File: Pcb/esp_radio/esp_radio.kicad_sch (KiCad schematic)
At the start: 0 parts

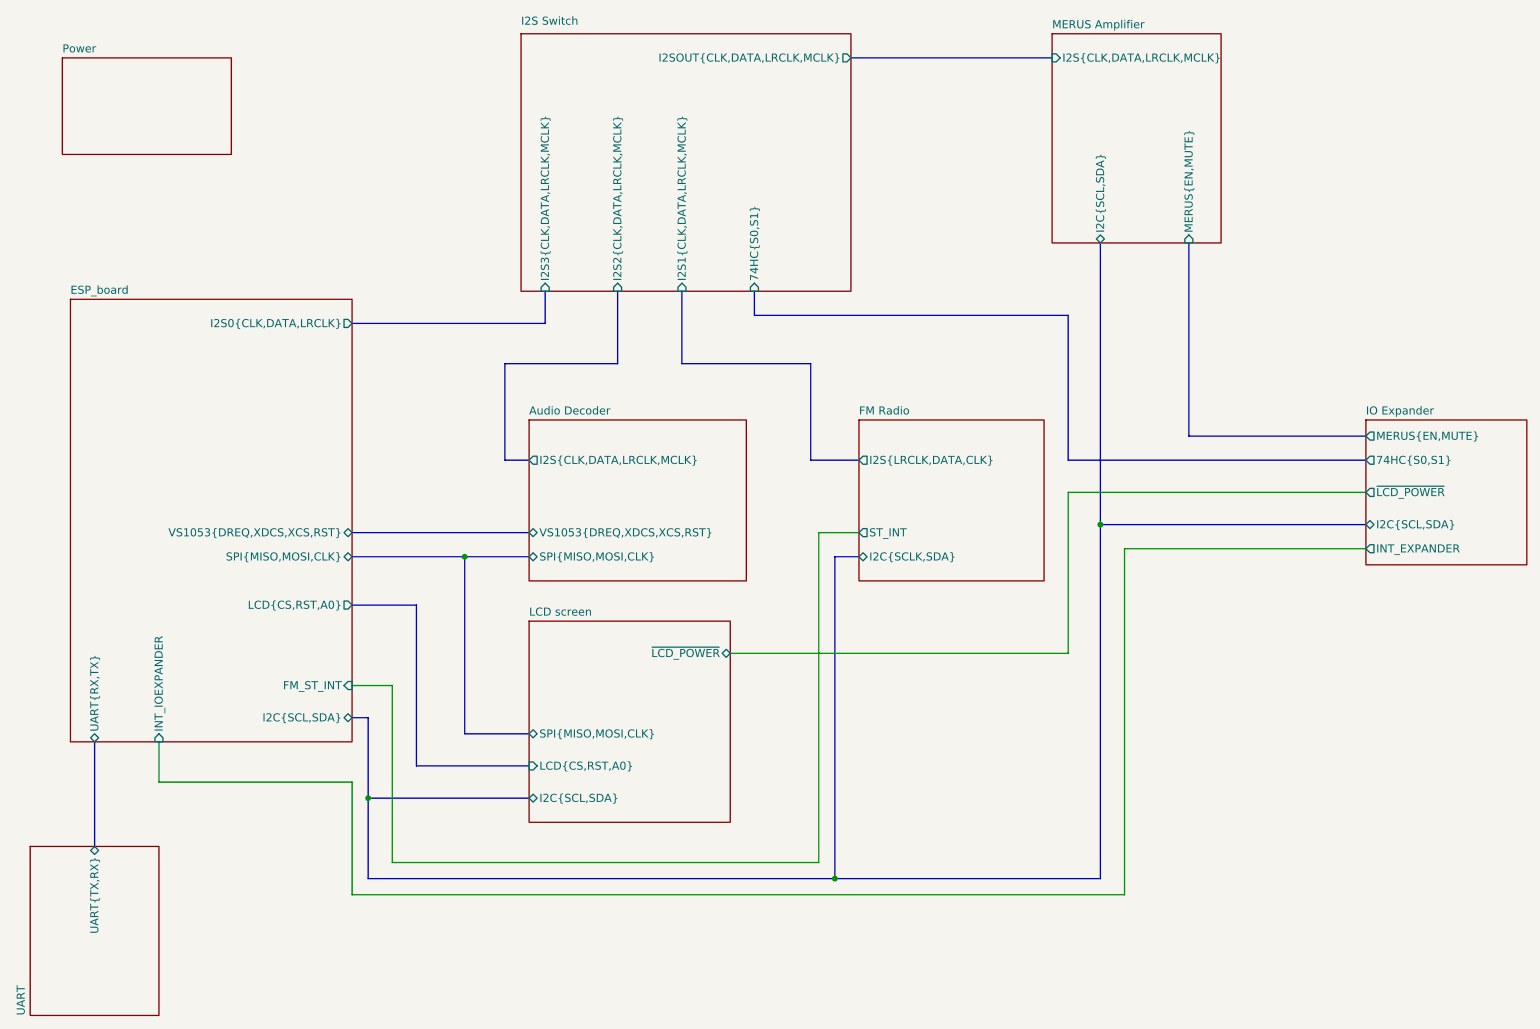
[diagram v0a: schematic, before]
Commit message: Move custom components to kicad_common_library.
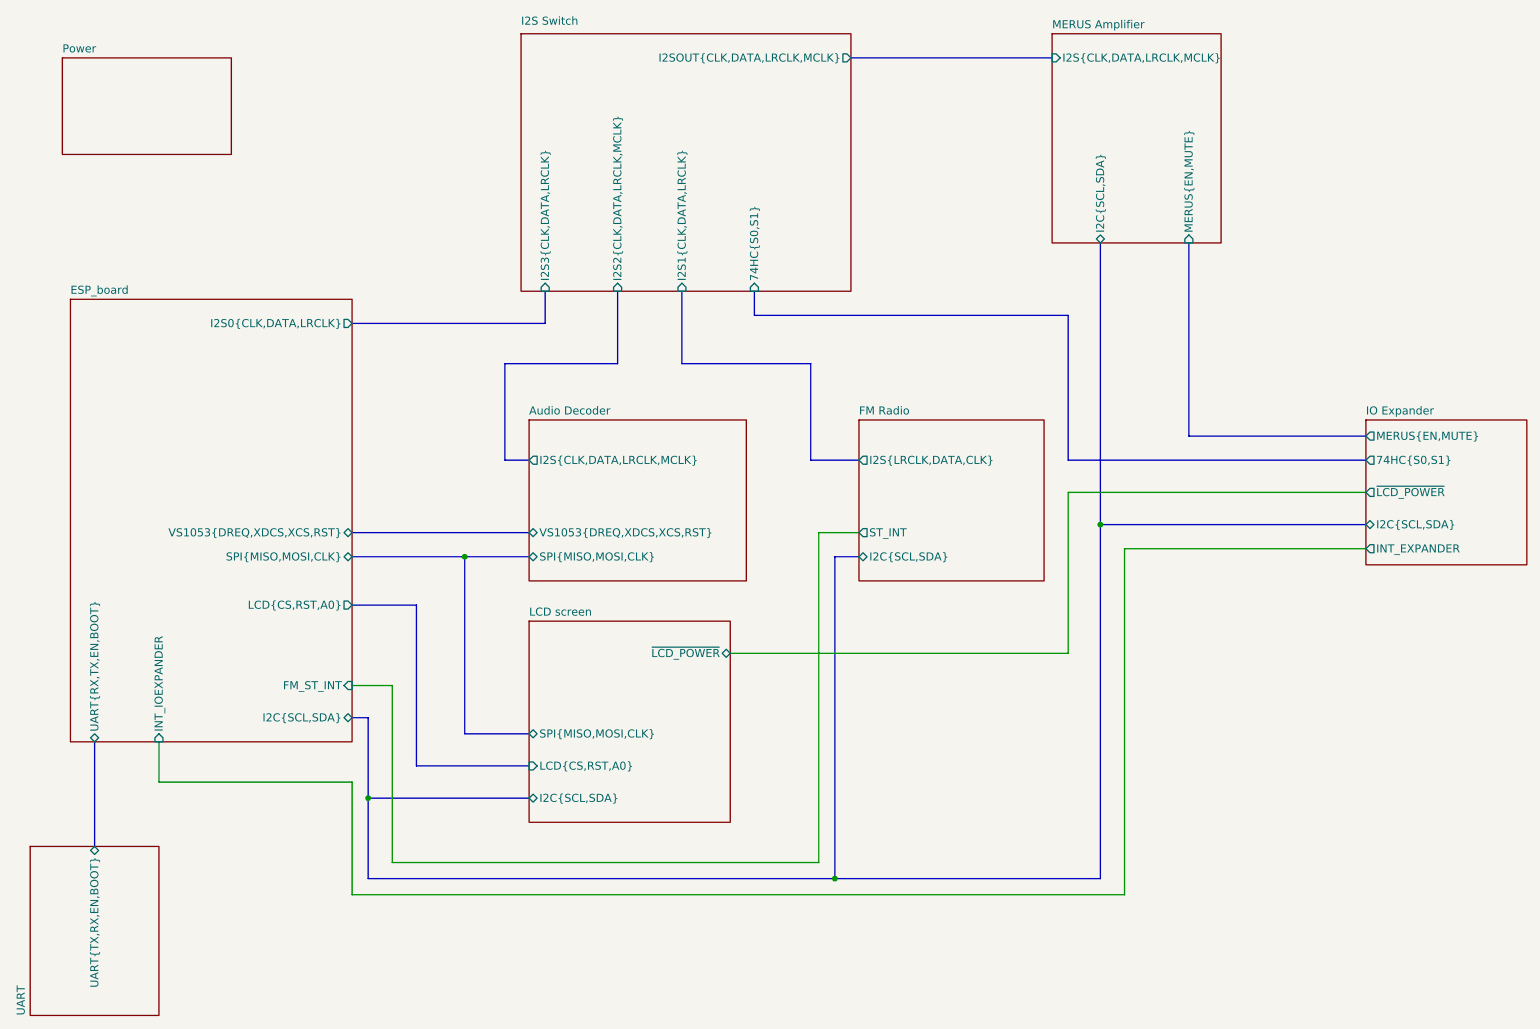
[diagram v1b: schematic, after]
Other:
- sheet ESP_board ports: added UART{RX,TX,EN,BOOT}; removed UART{RX,TX}
- sheet FM Radio ports: added I2C{SCL,SDA}; removed I2C{SCLK,SDA}
- sheet I2S Switch ports: added I2S1{CLK,DATA,LRCLK}, I2S3{CLK,DATA,LRCLK}; removed I2S1{CLK,DATA,LRCLK,MCLK}, I2S3{CLK,DATA,LRCLK,MCLK}
- sheet UART ports: added UART{TX,RX,EN,BOOT}; removed UART{TX,RX}
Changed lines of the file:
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@@
       (effects (font (size 1.27 1.27)) (justify right))
-    )
-    (pin "I2S3{CLK,DATA,LRCLK,MCLK}" input (at 128.27 57.15 270)
-      (effects (font (size 1.27 1.27)) (justify left))
     )
     (pin "74HC{S0,S1}" input (at 161.29 57.15 270)
@@
       (effects (font (size 1.27 1.27)) (justify left))
     )
-    (pin "I2S1{CLK,DATA,LRCLK,MCLK}" input (at 149.86 57.15 270)
+    (pin "I2S1{CLK,DATA,LRCLK}" input (at 149.86 57.15 270)
+      (effects (font (size 1.27 1.27)) (justify left))
+    )
+    (pin "I2S3{CLK,DATA,LRCLK}" input (at 128.27 57.15 270)
       (effects (font (size 1.27 1.27)) (justify left))
     )
@@
       (effects (font (size 1.27 1.27)) (justify left top) hide)
     )
-    (pin "I2C{SCLK,SDA}" bidirectional (at 177.8 99.06 180)
-      (effects (font (size 1.27 1.27)) (justify left))
-    )
     (pin "ST_INT" output (at 177.8 95.25 180)
       (effects (font (size 1.27 1.27)) (justify left))
     )
     (pin "I2S{LRCLK,DATA,CLK}" output (at 177.8 83.82 180)
+      (effects (font (size 1.27 1.27)) (justify left))
+    )
+    (pin "I2C{SCL,SDA}" bidirectional (at 177.8 99.06 180)
       (effects (font (size 1.27 1.27)) (justify left))
     )
@@
       (effects (font (size 1.27 1.27)) (justify left top) hide)
     )
-    (pin "UART{TX,RX}" bidirectional (at 57.15 144.78 90)
+    (pin "UART{TX,RX,EN,BOOT}" bidirectional (at 57.15 144.78 90)
       (effects (font (size 1.27 1.27)) (justify right))
     )
@@
       (effects (font (size 1.27 1.27)) (justify right))
     )
-    (pin "UART{RX,TX}" bidirectional (at 57.15 128.27 270)
-      (effects (font (size 1.27 1.27)) (justify left))
-    )
     (pin "I2S0{CLK,DATA,LRCLK}" output (at 97.79 62.23 0)
       (effects (font (size 1.27 1.27)) (justify right))
@@
       (effects (font (size 1.27 1.27)) (justify right))
     )
+    (pin "UART{RX,TX,EN,BOOT}" bidirectional (at 57.15 128.27 270)
+      (effects (font (size 1.27 1.27)) (justify left))
+    )
     (instances

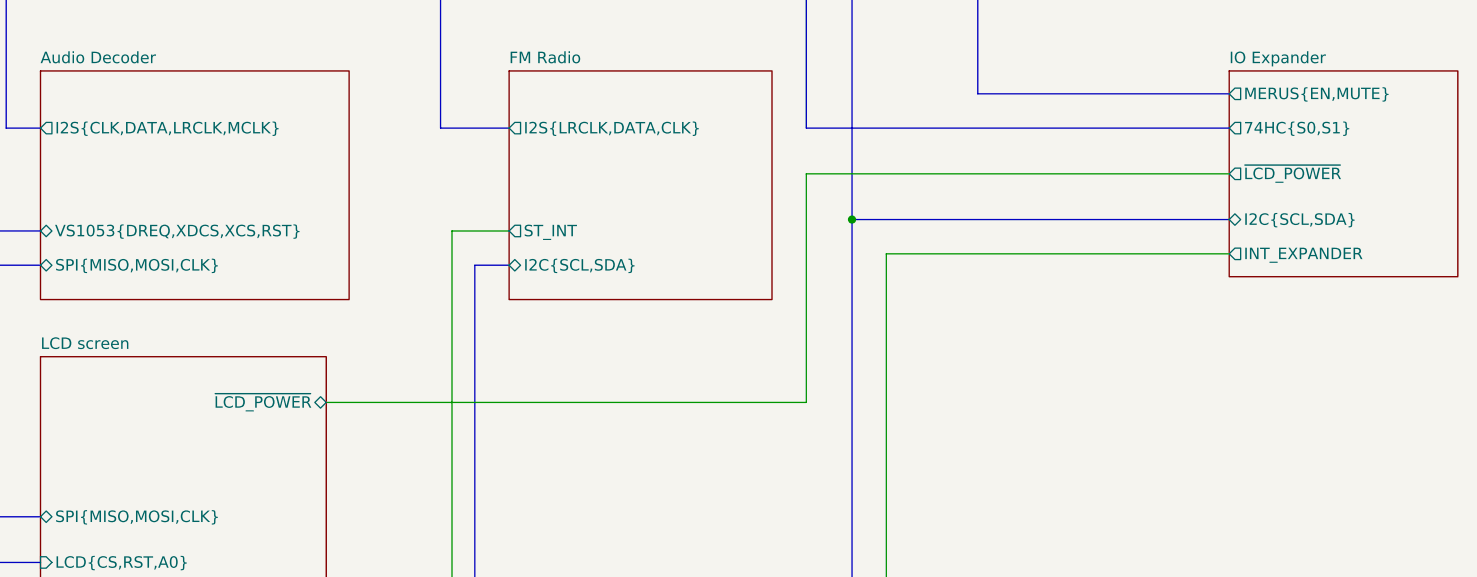
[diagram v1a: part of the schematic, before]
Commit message: Add components layout on PCB
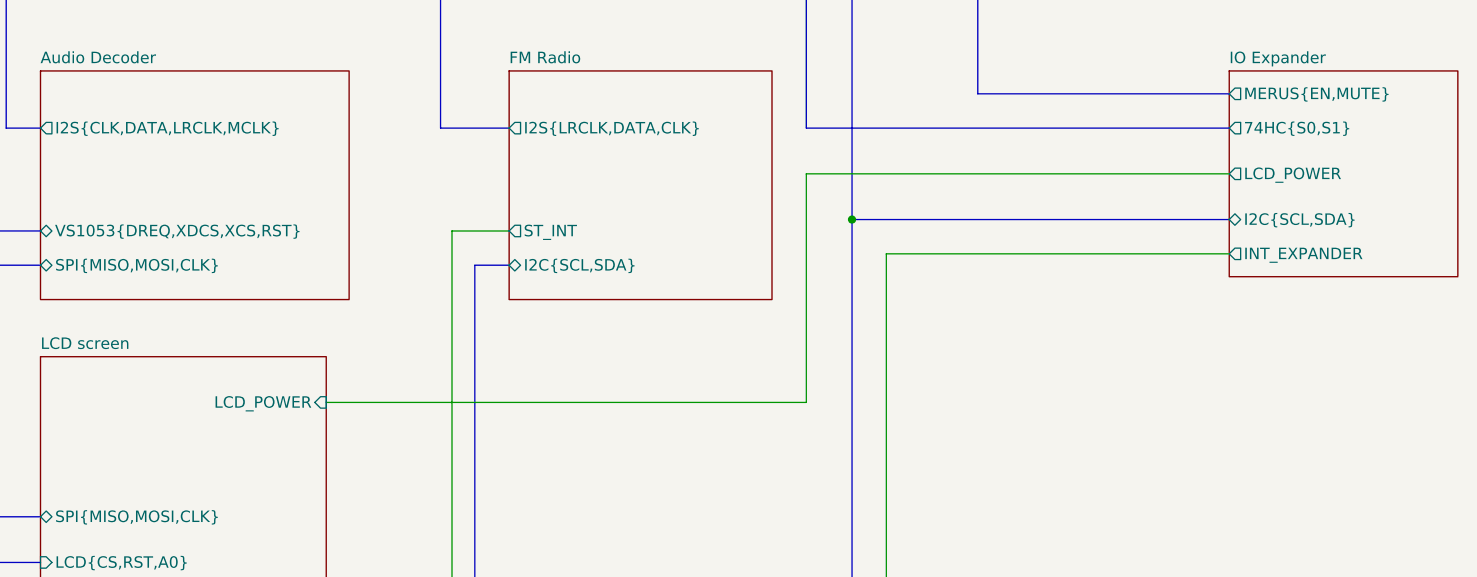
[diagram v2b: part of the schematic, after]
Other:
- sheet IO Expander ports: added LCD_POWER; removed ~{LCD_POWER}
- sheet LCD screen ports: added LCD_POWER; removed ~{LCD_POWER}
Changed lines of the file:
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@@
-      (effects (font (size 1.27 1.27)) (justify left))
-    )
-    (pin "~{LCD_POWER}" output (at 257.81 88.9 180)
       (effects (font (size 1.27 1.27)) (justify left))
     )
     (pin "MERUS{EN,MUTE}" output (at 257.81 80.01 180)
+      (effects (font (size 1.27 1.27)) (justify left))
+    )
+    (pin "LCD_POWER" output (at 257.81 88.9 180)
       (effects (font (size 1.27 1.27)) (justify left))
     )
@@
       (effects (font (size 1.27 1.27)) (justify left top) hide)
     )
-    (pin "~{LCD_POWER}" bidirectional (at 157.48 114.3 0)
-      (effects (font (size 1.27 1.27)) (justify right))
-    )
     (pin "I2C{SCL,SDA}" bidirectional (at 125.73 137.16 180)
       (effects (font (size 1.27 1.27)) (justify left))
@@
       (effects (font (size 1.27 1.27)) (justify left))
     )
+    (pin "LCD_POWER" input (at 157.48 114.3 0)
+      (effects (font (size 1.27 1.27)) (justify right))
+    )
     (instances

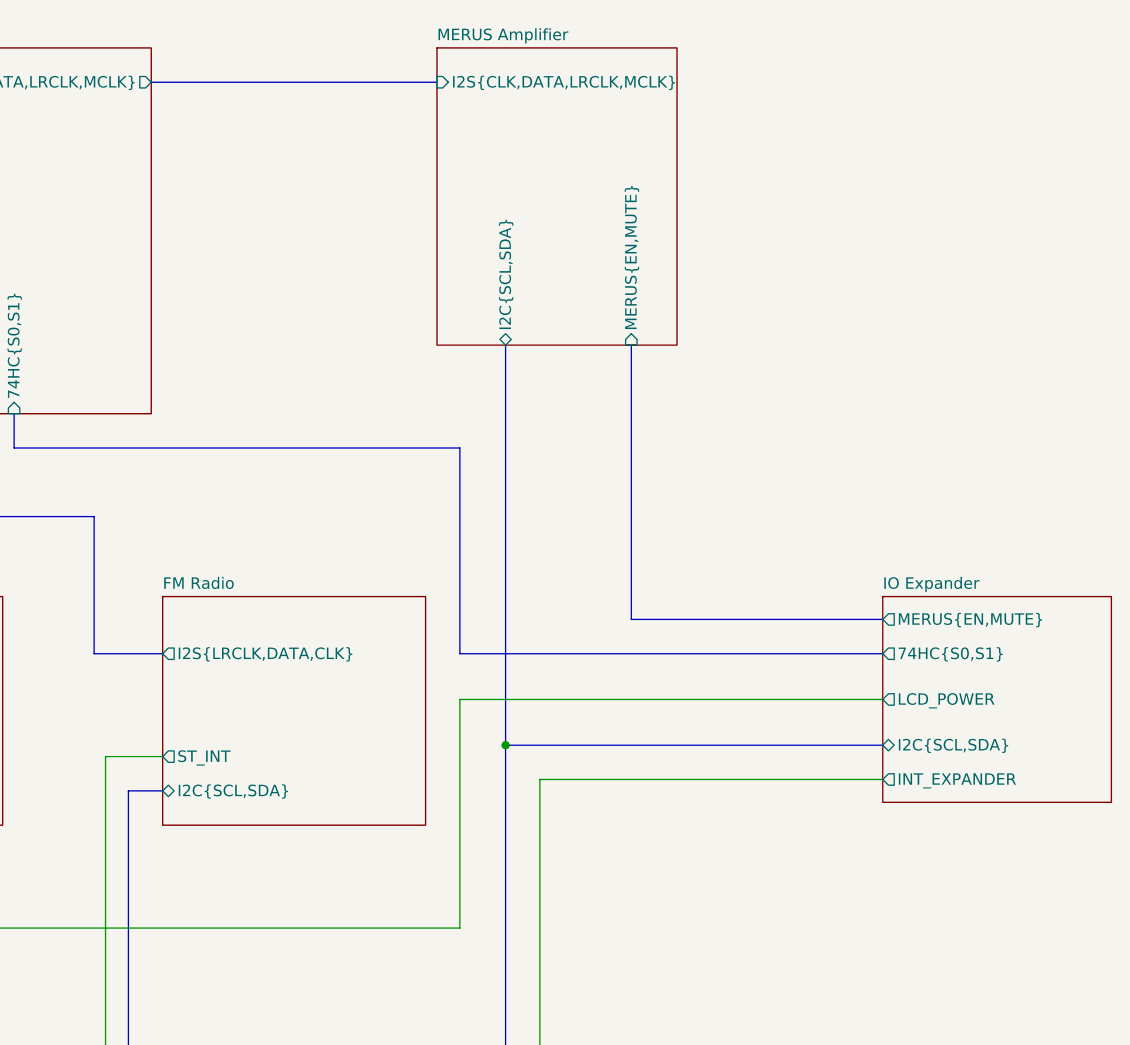
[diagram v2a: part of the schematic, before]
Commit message: Add chip select emulation for i2c devices
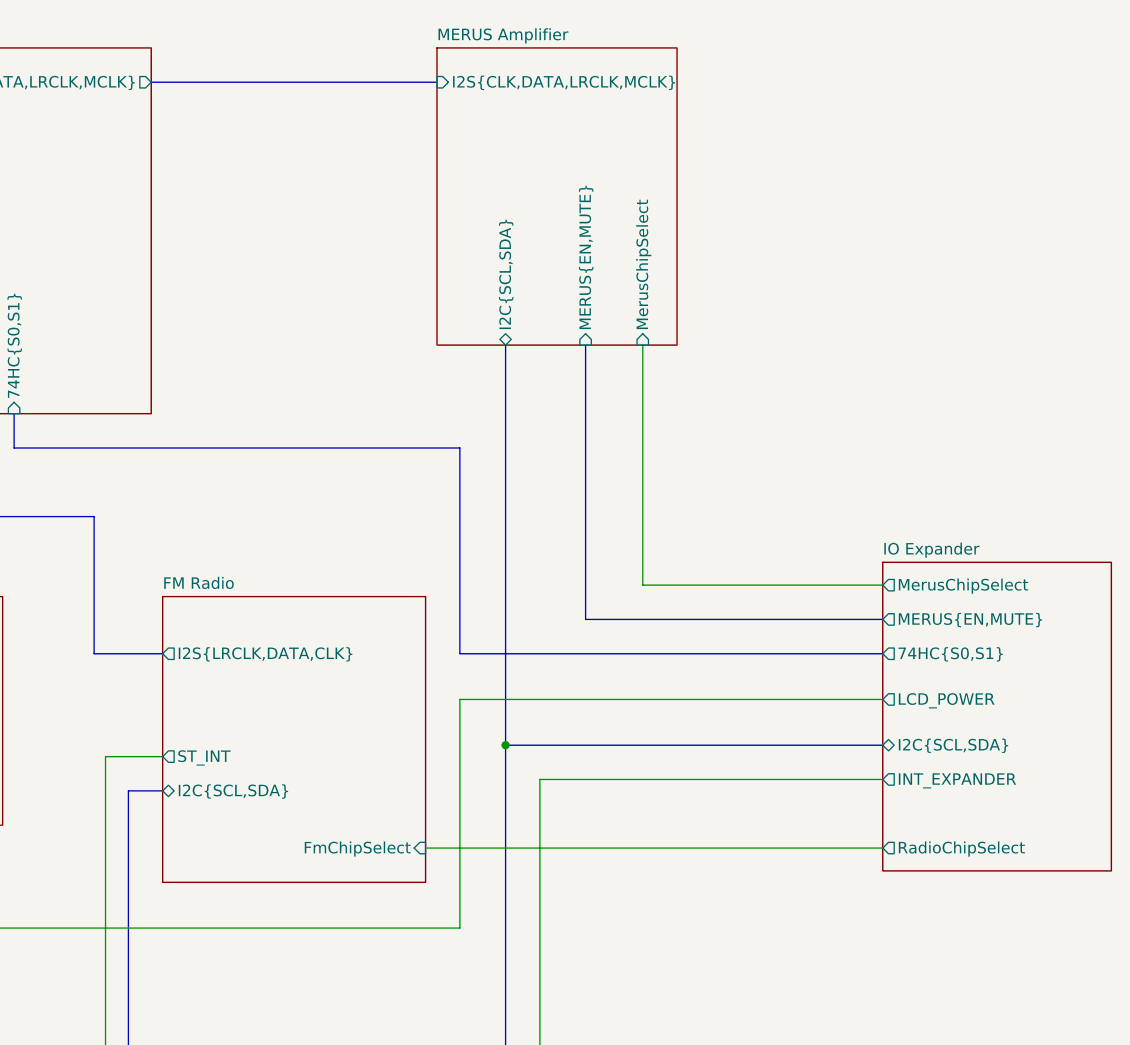
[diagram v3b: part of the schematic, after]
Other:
- sheet FM Radio ports: added FmChipSelect; removed none
- sheet IO Expander ports: added MerusChipSelect, RadioChipSelect; removed none
- sheet MERUS Amplifier ports: added MerusChipSelect; removed none
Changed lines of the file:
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@@
+    (stroke (width 0) (type default))
+  )
+  (wire (pts (xy 231.14 76.2) (xy 257.81 76.2))
     (stroke (width 0) (type default))
   )
@@
     (stroke (width 0) (type default))
   )
+  (wire (pts (xy 207.01 105.41) (xy 257.81 105.41))
+    (stroke (width 0) (type default))
+  )
   (bus (pts (xy 121.92 68.58) (xy 139.7 68.58))
     (stroke (width 0) (type default))
@@
     (stroke (width 0) (type default))
   )
-  (bus (pts (xy 257.81 80.01) (xy 229.87 80.01))
+  (bus (pts (xy 257.81 80.01) (xy 224.79 80.01))
     (stroke (width 0) (type default))
   )
@@
     (stroke (width 0) (type default))
   )
+  (wire (pts (xy 231.14 49.53) (xy 231.14 76.2))
+    (stroke (width 0) (type default))
+  )
   (bus (pts (xy 173.99 99.06) (xy 173.99 149.86))
     (stroke (width 0) (type default))
   )
-  (bus (pts (xy 229.87 80.01) (xy 229.87 49.53))
+  (bus (pts (xy 224.79 80.01) (xy 224.79 49.53))
     (stroke (width 0) (type default))
   )
@@
       (effects (font (size 1.27 1.27)) (justify left))
     )
-    (pin "MERUS{EN,MUTE}" input (at 229.87 49.53 270)
+    (pin "MERUS{EN,MUTE}" input (at 224.79 49.53 270)
       (effects (font (size 1.27 1.27)) (justify left))
     )
     (pin "I2C{SCL,SDA}" bidirectional (at 215.9 49.53 270)
+      (effects (font (size 1.27 1.27)) (justify left))
+    )
+    (pin "MerusChipSelect" input (at 231.14 49.53 270)
       (effects (font (size 1.27 1.27)) (justify left))
     )
@@
     )
   )
-  (sheet (at 177.8 77.47) (size 29.21 25.4) (fields_autoplaced)
+  (sheet (at 177.8 77.47) (size 29.21 31.75) (fields_autoplaced)
     (stroke (width 0.1524) (type solid))
     (fill (color 0 0 0 0.0000))
@@
       (effects (font (size 1.27 1.27)) (justify left bottom))
     )
-    (property "Sheetfile" "fm_radio.kicad_sch" (at 177.8 103.4546 0)
+    (property "Sheetfile" "fm_radio.kicad_sch" (at 177.8 109.8046 0)
       (effects (font (size 1.27 1.27)) (justify left top) hide)
     )
@@
       (effects (font (size 1.27 1.27)) (justify left))
     )
+    (pin "FmChipSelect" input (at 207.01 105.41 0)
+      (effects (font (size 1.27 1.27)) (justify right))
+    )
     (instances
       (project "esp_radio"
@@
     )
   )
-  (sheet (at 257.81 77.47) (size 25.4 22.86) (fields_autoplaced)
-    (stroke (width 0.1524) (type solid))
-    (fill (color 0 0 0 0.0000))
-    (property "Sheetname" "IO Expander" (at 257.81 76.7584 0)
-      (effects (font (size 1.27 1.27)) (justify left bottom))
-    )
-    (property "Sheetfile" "io_expander.kicad_sch" (at 257.81 100.9146 0)
+  (sheet (at 257.81 73.66) (size 25.4 34.29) (fields_autoplaced)
+    (stroke (width 0.1524) (type solid))
+    (fill (color 0 0 0 0.0000))
+    (property "Sheetname" "IO Expander" (at 257.81 72.9484 0)
+      (effects (font (size 1.27 1.27)) (justify left bottom))
+    )
+    (property "Sheetfile" "io_expander.kicad_sch" (at 257.81 108.5346 0)
       (effects (font (size 1.27 1.27)) (justify left top) hide)
     )
@@
       (effects (font (size 1.27 1.27)) (justify left))
     )
+    (pin "MerusChipSelect" output (at 257.81 76.2 180)
+      (effects (font (size 1.27 1.27)) (justify left))
+    )
+    (pin "RadioChipSelect" output (at 257.81 105.41 180)
+      (effects (font (size 1.27 1.27)) (justify left))
+    )
